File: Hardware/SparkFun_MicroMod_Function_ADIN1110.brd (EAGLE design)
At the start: 38 x 65 mm, 113 parts, among them J1 T1_INDUSTRIAL, J2 MICROMOD_FUNCTION_STANDARD, Q1 220mA/50V/3.5Ω, Q2 20V/4.2A/52mΩ/1.4W, T1 WE-STST, U1 ADIN1110, U2 EEPROM, U3 3.3V, U4 WE-TVS, Y1 25MHz

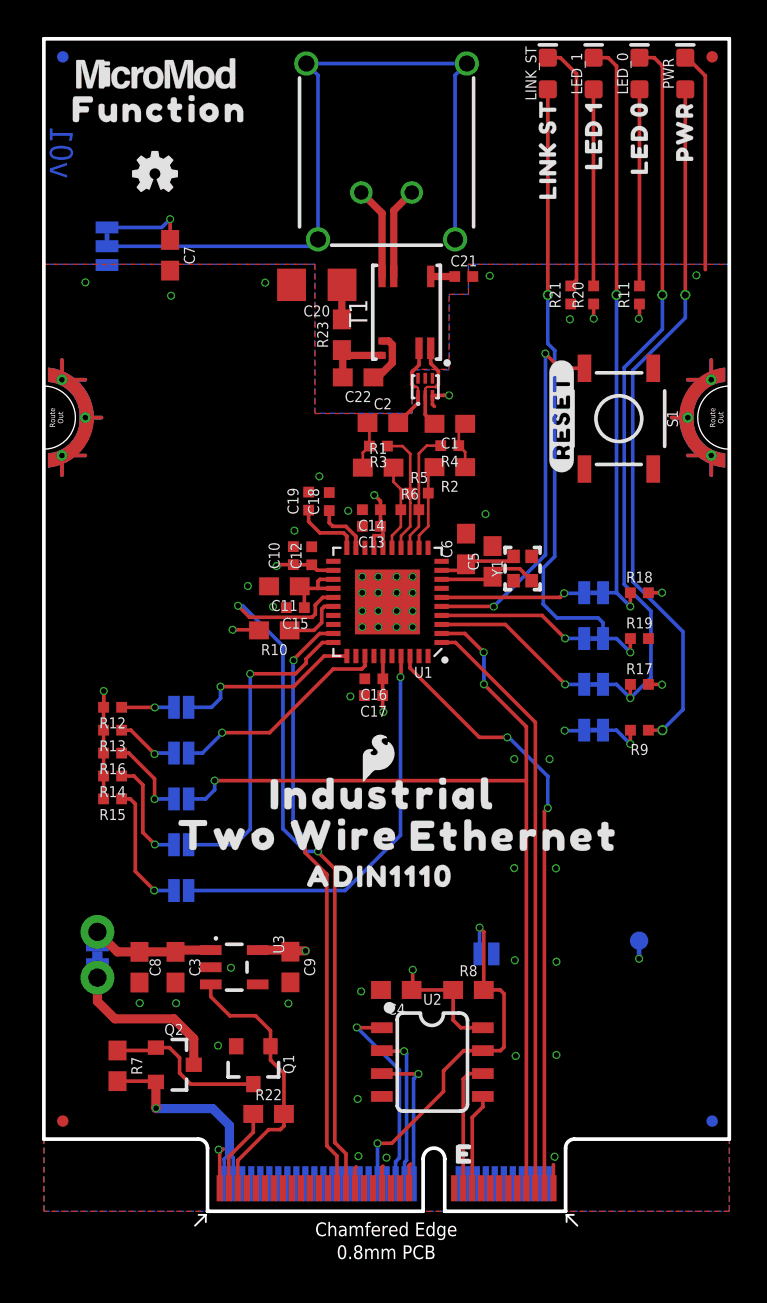
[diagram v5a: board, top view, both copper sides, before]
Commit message: checklist catches
-added CS and INT pulllups
-nudged vias to avoid silk
-added 1/2/3/4 text objects to help indicate 4 layers
-added suggested Selective Solder path on layer 48
-adjusted tnames for better assembly sheet
-added measures
-corrected active low labels on some bottom config jumpers
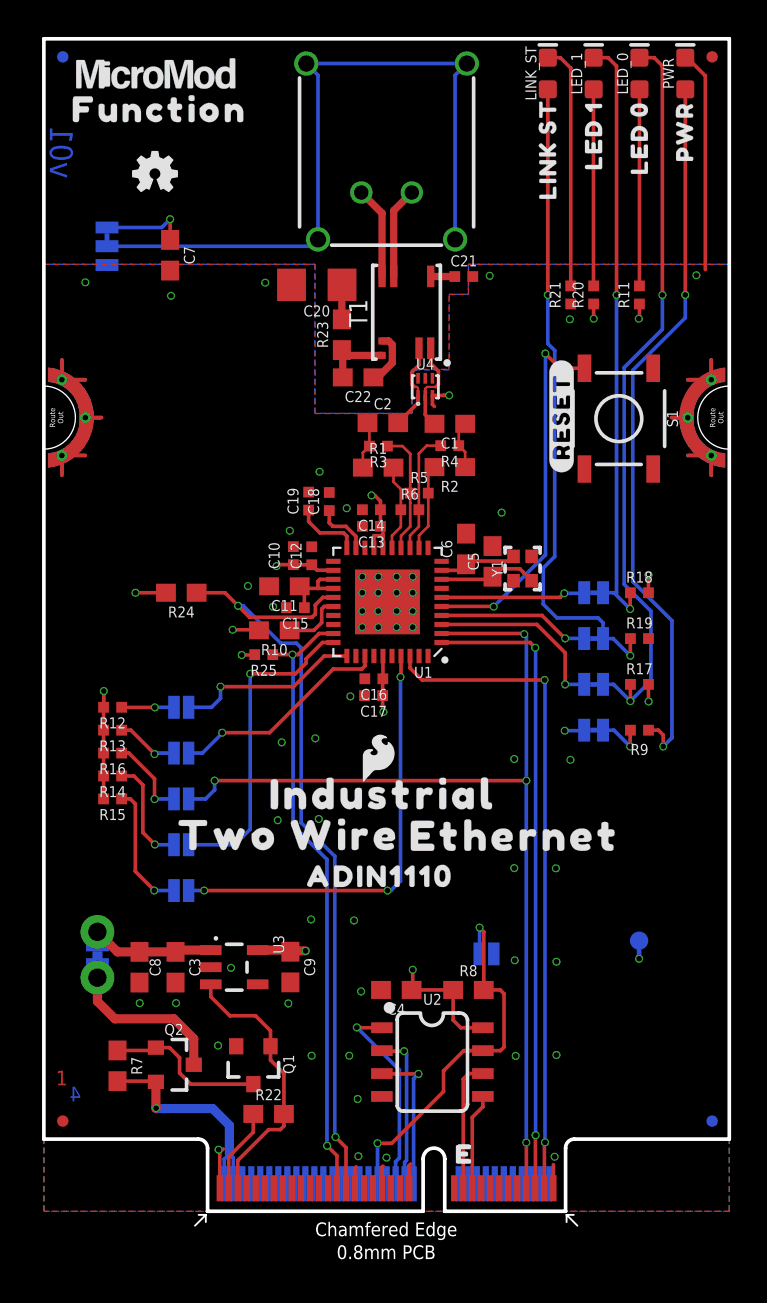
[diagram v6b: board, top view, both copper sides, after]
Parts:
- removed U$17: (no value), output:#SWPD_EN#1
- removed U$18: (no value), output:#TX2P4_EN#2
- added R24: 1.5k, SparkFun-Resistors:0603
- added R25: 4.7k, SparkFun-Resistors:0402-TIGHT
- added U$13: (no value), output:##TX2P4_EN##4
- added U$22: (no value), output:##SWPD_EN##4
- moved FRAME1 46.7 mm to (-7.62, -26.7)
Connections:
- net !MS_SEL! renamed MS_SEL
- net !CS!: now also R25.1
- net !INT!: now also R24.1
- net 3.3V: now also R24.2, R25.2
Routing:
- net 3.3V: track 33.2 -> 36.2 mm, vias 13 -> 15
- net SPI_SCK: track 33.7 -> 36.6 mm
- net !INT!: track 41.6 -> 44.3 mm
- net SPI_COPI: track 32.9 -> 35.3 mm, vias 0 -> 2
- net SPI_CIPO/SPI_CFG0: track 52.9 -> 54.8 mm, vias 3 -> 4
- net SPI_CFG1: track 23.0 -> 24.4 mm, vias 1 -> 3
- net !CS!: track 33.1 -> 34.5 mm
- net N$20: track 39.1 -> 40.3 mm
- net LED_0: track 9.29 -> 10.3 mm
- net GND: vias 49 -> 57
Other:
- board text added: "1"
- board text added: "2"
- board text added: "3"
- board text added: "4"
- board text added: "UNITS IN INCHES"

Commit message: connected RESET to MM GPIO (F5)
-needed for testing, but also could be useful for the user to perform a hard reset on the ANIN1110 from GPIO controlled on their MM main board.
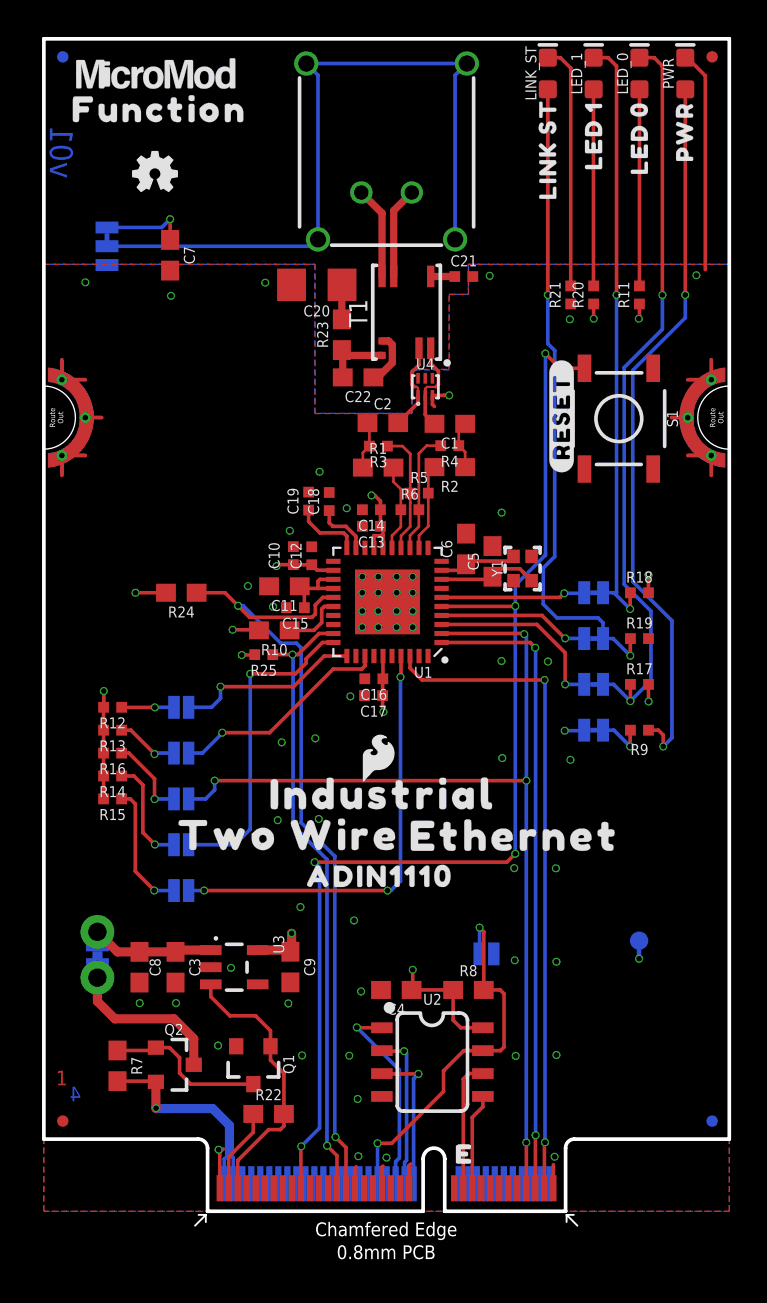
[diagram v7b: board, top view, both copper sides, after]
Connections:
- net !RESET!: now also J2.57
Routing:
- net !RESET!: track 20.6 -> 65.0 mm, vias 2 -> 5
- net GND: vias 57 -> 59
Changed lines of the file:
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@@
 <drawing>
 <settings>
-<setting alwaysvectorfont="yes"/>
+<setting alwaysvectorfont="no"/>
 <setting verticaltext="up"/>
 </settings>
@@
 <via x="26.076459375" y="19.023003125" extent="1-16" drill="0.3048"/>
 <via x="29.192159375" y="25.027440625" extent="1-16" drill="0.3048"/>
-<via x="26.076459375" y="25.073003125" extent="1-16" drill="0.3048"/>
+<via x="25.413521875" y="25.123803125" extent="1-16" drill="0.3048"/>
 <via x="16.93058125" y="8.624903125" extent="1-16" drill="0.3048"/>
-<via x="14.845240625" y="8.624903125" extent="1-16" drill="0.3048"/>
+<via x="14.314378125" y="8.642684375" extent="1-16" drill="0.3048"/>
 <via x="17.197278125" y="16.122984375" extent="1-16" drill="0.3048"/>
-<via x="14.814759375" y="16.181403125" extent="1-16" drill="0.3048"/>
+<via x="14.22548125" y="16.867203125" extent="1-16" drill="0.3048"/>
 <via x="15.241478125" y="21.74654375" extent="1-16" drill="0.3048"/>
 <via x="12.9631" y="21.680503125" extent="1-16" drill="0.3048"/>
 <via x="15.0459" y="26.21694375" extent="1-16" drill="0.3048"/>
 <via x="13.186621875" y="25.9959625" extent="1-16" drill="0.3048"/>
+<via x="27.94501875" y="30.475740625" extent="1-16" drill="0.3048"/>
+<via x="25.369459375" y="30.506221875" extent="1-16" drill="0.3048"/>
 </signal>
 <signal name="3.3V">
@@
 <contactref element="R18" pad="2"/>
 <contactref element="R20" pad="1"/>
-<via x="14.50758125" y="14.437678125" extent="1-16" drill="0.3048"/>
+<via x="13.735421875" y="15.407959375" extent="1-16" drill="0.3048"/>
 <via x="12.900659375" y="35.765740625" extent="1-16" drill="0.3048"/>
 <via x="18.16608125" y="39.684965625" extent="1-16" drill="0.3048"/>
@@
 <wire x1="11.8551" y1="14.48" x2="13.578" y2="14.48" width="0.508" layer="1"/>
 <wire x1="13.578" y1="14.48" x2="13.668" y2="14.39" width="0.508" layer="1"/>
-<wire x1="13.668" y1="14.39" x2="13.715678125" y2="14.437678125" width="0.508" layer="1"/>
-<wire x1="13.715678125" y1="14.437678125" x2="14.50758125" y2="14.437678125" width="0.508" layer="1"/>
+<wire x1="13.668" y1="14.39" x2="13.735425" y2="14.457425" width="0.508" layer="1"/>
 <wire x1="20.4495375" y1="13.3858" x2="20.4495375" y2="12.3295375" width="0.2032" layer="1"/>
 <wire x1="20.4495375" y1="12.3295375" x2="20.39" y2="12.27" width="0.2032" layer="1"/>
@@
 <wire x1="11.692" y1="30.861" x2="11.67168125" y2="30.84068125" width="0.2032" layer="1"/>
 <wire x1="11.67168125" y1="30.84068125" x2="10.9728" y2="30.84068125" width="0.2032" layer="1"/>
+<wire x1="13.735425" y1="14.457425" x2="13.735425" y2="15.40795625" width="0.508" layer="1"/>
+<wire x1="13.735425" y1="15.40795625" x2="13.735421875" y2="15.407959375" width="0.508" layer="1"/>
 </signal>
 <signal name="SPI_COPI">
@@
 <contactref element="U1" pad="5"/>
 <contactref element="S1" pad="3"/>
-<wire x1="22.05" y1="33.532" x2="24.929090625" y2="33.532" width="0.2032" layer="1"/>
-<wire x1="24.929090625" y1="33.532" x2="24.940140625" y2="33.52095" width="0.2032" layer="1"/>
-<via x="24.940140625" y="33.52095" extent="1-16" drill="0.3048"/>
+<wire x1="22.05" y1="33.532" x2="26.117053125" y2="33.532" width="0.2032" layer="1"/>
+<wire x1="26.117053125" y1="33.532" x2="26.139021875" y2="33.55396875" width="0.2032" layer="1"/>
+<via x="26.139021875" y="33.55396875" extent="1-16" drill="0.3048"/>
 <wire x1="27.8003" y1="47.551340625" x2="27.810140625" y2="47.5415" width="0.2032" layer="16"/>
-<wire x1="27.810140625" y1="47.5415" x2="27.810140625" y2="36.39095" width="0.2032" layer="16"/>
-<wire x1="24.940140625" y1="33.52095" x2="27.810140625" y2="36.39095" width="0.2032" layer="16"/>
+<wire x1="27.810140625" y1="47.5415" x2="27.810140625" y2="36.378246875" width="0.2032" layer="16"/>
+<wire x1="26.139021875" y1="33.55396875" x2="26.139021875" y2="34.707128125" width="0.2032" layer="16"/>
+<wire x1="27.810140625" y1="36.378246875" x2="26.139021875" y2="34.707128125" width="0.2032" layer="16"/>
 <via x="27.8003" y="47.551340625" extent="1-16" drill="0.3048"/>
 <wire x1="27.8003" y1="47.551340625" x2="28.615640625" y2="46.736" width="0.2032" layer="1"/>
 <wire x1="28.615640625" y1="46.736" x2="29.972" y2="46.736" width="0.2032" layer="1"/>
+<contactref element="J2" pad="57"/>
+<wire x1="14.25" y1="1.275" x2="14.25" y2="3.579459375" width="0.2032" layer="1"/>
+<wire x1="14.25" y1="3.579459375" x2="14.26718125" y2="3.596640625" width="0.2032" layer="1"/>
+<via x="14.26718125" y="3.596640625" extent="1-16" drill="0.3048"/>
+<wire x1="14.26718125" y1="3.596640625" x2="15.28571875" y2="4.615178125" width="0.2032" layer="16"/>
+<wire x1="15.28571875" y1="19.08048125" x2="15.0114" y2="19.3548" width="0.2032" layer="16"/>
+<via x="15.0114" y="19.3548" extent="1-16" drill="0.3048"/>
+<wire x1="15.0114" y1="19.3548" x2="25.669240625" y2="19.3548" width="0.2032" layer="1"/>
+<wire x1="25.669240625" y1="19.3548" x2="26.134059375" y2="19.81961875" width="0.2032" layer="1"/>
+<via x="26.134059375" y="19.81961875" extent="1-16" drill="0.3048"/>
+<wire x1="15.28571875" y1="4.615178125" x2="15.28571875" y2="19.08048125" width="0.2032" layer="16"/>
+<wire x1="26.134059375" y1="33.54900625" x2="26.139021875" y2="33.55396875" width="0.2032" layer="16"/>
+<wire x1="26.134059375" y1="19.81961875" x2="26.134059375" y2="33.54900625" width="0.2032" layer="16"/>
 </signal>
 <signal name="1.1V">

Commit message: Final tweaks before ordering protos
-pulled GND back out to LEDS
-reverted back to T1 connector max tolerance drill size
-added connector width to measures
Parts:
- moved FRAME1 11.9 mm to (-6.72, -14.8)
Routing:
- net GND: track 21.7 -> 9.56 mm, vias 59 -> 64
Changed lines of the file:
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@@
 <drawing>
 <settings>
-<setting alwaysvectorfont="no"/>
+<setting alwaysvectorfont="yes"/>
 <setting verticaltext="up"/>
 </settings>
-<grid distance="0.05" unitdist="inch" unit="inch" style="lines" multiple="1" display="yes" altdistance="0.0001" altunitdist="inch" altunit="inch"/>
+<grid distance="0.1" unitdist="mm" unit="mm" style="lines" multiple="1" display="yes" altdistance="0.001" altunitdist="inch" altunit="inch"/>
 <layers>
 <layer number="1" name="Top/Horz" color="4" fill="1" visible="yes" active="yes"/>
@@
 <layer number="45" name="Holes" color="7" fill="1" visible="yes" active="yes"/>
 <layer number="46" name="Milling" color="3" fill="1" visible="no" active="yes"/>
-<layer number="47" name="Measures" color="7" fill="1" visible="no" active="yes"/>
+<layer number="47" name="Measures" color="7" fill="1" visible="yes" active="yes"/>
 <layer number="48" name="Document" color="7" fill="1" visible="no" active="yes"/>
 <layer number="49" name="Reference" color="7" fill="1" visible="yes" active="yes"/>
@@
 <layer number="98" name="Guide" color="6" fill="1" visible="no" active="no"/>
 <layer number="99" name="SpiceOrder" color="7" fill="1" visible="no" active="no"/>
-<layer number="100" name="Muster" color="7" fill="1" visible="no" active="yes"/>
+<layer number="100" name="Muster" color="7" fill="1" visible="yes" active="yes"/>
 <layer number="101" name="Patch_Top" color="12" fill="4" visible="no" active="no"/>
 <layer number="102" name="Vscore" color="7" fill="1" visible="no" active="no"/>
@@
 <wire x1="28.925" y1="0" x2="22.225" y2="0" width="0.2032" layer="20"/>
 <text x="0.9686" y="58.713278125" size="1.27" layer="16" font="vector" ratio="20" rot="SMR90" align="center">v01</text>
-<text x="19.05" y="-26.67" size="1.778" layer="51" font="vector" ratio="10">Pete Lewis</text>
+<text x="19.95" y="-14.77" size="1.778" layer="51" font="vector" ratio="10">Pete Lewis</text>
 <wire x1="21.025" y1="0" x2="9.075" y2="0" width="0.2032" layer="20"/>
 <wire x1="28.925" y1="0" x2="28.925" y2="3.5" width="0.2032" layer="20"/>
@@
 <text x="46.99" y="43.18" size="1.778" layer="51" font="vector" ratio="15">Beveled Edge</text>
 <text x="46.99" y="40.64" size="1.778" layer="51" font="vector" ratio="15">ENIG Finish</text>
-<text x="3.81" y="-27.559" size="1.778" layer="51" font="vector" ratio="10" align="top-left">Based off the MicroMod PoE Ethernet
+<text x="4.71" y="-15.659" size="1.778" layer="51" font="vector" ratio="10" align="top-left">Based off the MicroMod PoE Ethernet
 function board by N. Seidle</text>
 <text x="0.670559375" y="6.982459375" size="0.8128" layer="1" font="vector" ratio="25">1</text>
@@
 <wire x1="23.154640625" y1="54.841140625" x2="23.154640625" y2="65.89268125" width="6.6802" layer="48"/>
 <dimension x1="0" y1="0" x2="0" y2="65" x3="-12.0523" y3="32.5" textsize="1.778" textratio="15" layer="47" dtype="vertical" unit="inch"/>
-<text x="7.62" y="-16.51" size="1.778" layer="47" font="vector" ratio="15">UNITS IN INCHES</text>
-<dimension x1="0" y1="65" x2="38" y2="65" x3="19" y3="89.308940625" textsize="1.778" textratio="15" layer="47" dtype="horizontal" unit="inch"/>
-<dimension x1="0" y1="65" x2="19" y2="65" x3="9.5" y3="70.65771875" textsize="1.778" textratio="15" layer="47" dtype="horizontal" unit="inch"/>
-<dimension x1="0" y1="65" x2="35.560040625" y2="63.0764" x3="17.78001875" y3="85.6615" textsize="1.778" textratio="15" layer="47" dtype="horizontal" unit="inch"/>
-<dimension x1="0" y1="65" x2="33.020040625" y2="63.0764" x3="16.51001875" y3="82.4357" textsize="1.778" textratio="15" layer="47" dtype="horizontal" unit="inch"/>
-<dimension x1="0" y1="65" x2="30.480040625" y2="63.0764" x3="15.24001875" y3="78.729840625" textsize="1.778" textratio="15" layer="47" dtype="horizontal" unit="inch"/>
-<dimension x1="0" y1="65" x2="27.940040625" y2="63.0764" x3="13.97001875" y3="74.983340625" textsize="1.778" textratio="15" layer="47" dtype="horizontal" unit="inch"/>
+<text x="8.42" y="-5.01" size="1.778" layer="47" font="vector" ratio="15">UNITS IN INCHES</text>
+<dimension x1="0" y1="65" x2="38" y2="65" x3="19" y3="98.198940625" textsize="1.778" textratio="15" layer="47" dtype="horizontal" unit="inch"/>
+<dimension x1="0" y1="65" x2="19" y2="65" x3="9.5" y3="74.46771875" textsize="1.778" textratio="15" layer="47" dtype="horizontal" unit="inch"/>
+<dimension x1="0" y1="65" x2="35.560040625" y2="63.0764" x3="17.78001875" y3="94.5515" textsize="1.778" textratio="15" layer="47" dtype="horizontal" unit="inch"/>
+<dimension x1="0" y1="65" x2="33.020040625" y2="63.0764" x3="16.51001875" y3="91.3257" textsize="1.778" textratio="15" layer="47" dtype="horizontal" unit="inch"/>
+<dimension x1="0" y1="65" x2="30.480040625" y2="63.0764" x3="15.24001875" y3="87.619840625" textsize="1.778" textratio="15" layer="47" dtype="horizontal" unit="inch"/>
+<dimension x1="0" y1="65" x2="27.940040625" y2="63.0764" x3="13.97001875" y3="83.873340625" textsize="1.778" textratio="15" layer="47" dtype="horizontal" unit="inch"/>
 <dimension x1="0" y1="0" x2="0.027940625" y2="44.071540625" x3="-7.4549" y3="22.03576875" textsize="1.778" textratio="15" layer="47" dtype="vertical" unit="inch"/>
 <dimension x1="0" y1="0" x2="0" y2="4" x3="-2.9972" y3="2" textsize="1.778" textratio="15" layer="47" dtype="vertical" unit="inch"/>
+<dimension x1="14.4018" y1="68.7324" x2="23.5966" y2="68.7324" x3="18.9992" y3="79.1972" textsize="1.778" textratio="15" layer="100" dtype="horizontal" unit="inch"/>
 </plain>
 <attributes>
@@
 <attribute name="VALUE" x="9.77138125" y="15.229840625" size="0.6096" layer="27" ratio="20"/>
 </element>
-<element name="FRAME1" library="SparkFun-Aesthetics" package="CREATIVE_COMMONS" value="FRAME-LEDGER" x="-7.62" y="-26.67" smashed="yes">
-<attribute name="DESIGNER" value="" x="-7.62" y="-26.67" size="1.778" layer="27" font="vector" ratio="15" display="off"/>
-<attribute name="REV" value="" x="-7.62" y="-26.67" size="1.778" layer="27" font="vector" ratio="15" display="off"/>
+<element name="FRAME1" library="SparkFun-Aesthetics" package="CREATIVE_COMMONS" value="FRAME-LEDGER" x="-6.72" y="-14.77" smashed="yes">
+<attribute name="DESIGNER" value="" x="-6.72" y="-14.77" size="1.778" layer="27" font="vector" ratio="15" display="off"/>
+<attribute name="REV" value="" x="-6.72" y="-14.77" size="1.778" layer="27" font="vector" ratio="15" display="off"/>
 </element>
 <element name="C9" library="SparkFun-Capacitors" package="0603" value="1.0uF" x="13.668" y="13.54" smashed="yes" rot="R270">
@@
 <vertex x="23.53818125" y="50.835559375"/>
 <vertex x="23.53818125" y="52.49903125"/>
-<vertex x="38" y="52.49903125"/>
+<vertex x="26.7" y="52.49903125"/>
+<vertex x="26.7" y="65"/>
+<vertex x="38" y="65"/>
 <vertex x="38" y="0"/>
 </polygon>
@@
 <vertex x="0" y="0"/>
 <vertex x="38" y="0"/>
-<vertex x="38" y="52.499965625"/>
+<vertex x="38" y="65"/>
+<vertex x="26.7" y="65"/>
+<vertex x="26.7" y="52.498996875"/>
 <vertex x="23.53818125" y="52.498996875"/>
 <vertex x="23.53818125" y="50.83048125"/>
@@
 <via x="2.3" y="51.5" extent="1-16" drill="0.3048"/>
 <wire x1="35.560040625" y1="63.9534" x2="35.6666" y2="63.9534" width="0.2032" layer="1"/>
-<wire x1="36.67" y1="62.95" x2="36.67" y2="52.2" width="0.2032" layer="1"/>
-<wire x1="35.6666" y1="63.9534" x2="36.67" y2="62.95" width="0.2032" layer="1"/>
 <via x="29.161740625" y="49.44871875" extent="1-16" drill="0.3048"/>
 <via x="24.716740625" y="51.86171875" extent="1-16" drill="0.3048"/>
@@
 <via x="27.94501875" y="30.475740625" extent="1-16" drill="0.3048"/>
 <via x="25.369459375" y="30.506221875" extent="1-16" drill="0.3048"/>
+<via x="37.06368125" y="62.17665625" extent="1-16" drill="0.3048"/>
+<via x="27.03068125" y="62.93865625" extent="1-16" drill="0.3048"/>
+<via x="36.80968125" y="56.84265625" extent="1-16" drill="0.3048"/>
+<via x="27.03068125" y="56.71565625" extent="1-16" drill="0.3048"/>
+<via x="32.36468125" y="56.71565625" extent="1-16" drill="0.3048"/>
 </signal>
 <signal name="3.3V">
